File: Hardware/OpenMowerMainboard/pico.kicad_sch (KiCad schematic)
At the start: 3 parts, among them U10 74HC4051, U11 Pico, U9 74HC4051

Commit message: wip schematic
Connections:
- net USS_ADDRESS_0 renamed MUX_ADDRESS_0
- net USS_ADDRESS_1 renamed MUX_ADDRESS_1
- net USS_ADDRESS_2 renamed MUX_ADDRESS_2
- net USS_ECHO renamed MUX_INPUT
- net USS_TRIGGER renamed MUX_OUTPUT
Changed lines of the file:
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@@
     (stroke (width 0) (type default) (color 0 0 0 0))
   )
-  (label "USS_ADDRESS_0" (at 173.99 88.9 0)
+  (label "MUX_ADDRESS_0" (at 173.99 88.9 0)
     (effects (font (size 1.27 1.27)) (justify left bottom))
   )
-  (label "USS_TRIGGER" (at 69.85 86.36 0)
+  (label "MUX_OUTPUT" (at 69.85 86.36 0)
     (effects (font (size 1.27 1.27)) (justify left bottom))
   )
-  (label "USS_ADDRESS_2" (at 131.445 96.52 0)
+  (label "MUX_ADDRESS_2" (at 131.445 96.52 0)
     (effects (font (size 1.27 1.27)) (justify left bottom))
   )
-  (label "USS_ADDRESS_0" (at 131.445 91.44 0)
+  (label "MUX_ADDRESS_0" (at 131.445 91.44 0)
     (effects (font (size 1.27 1.27)) (justify left bottom))
   )
-  (label "USS_ADDRESS_0" (at 69.85 91.44 0)
+  (label "MUX_ADDRESS_0" (at 69.85 91.44 0)
     (effects (font (size 1.27 1.27)) (justify left bottom))
   )
-  (label "USS_ADDRESS_2" (at 69.85 96.52 0)
+  (label "MUX_ADDRESS_2" (at 69.85 96.52 0)
     (effects (font (size 1.27 1.27)) (justify left bottom))
   )
-  (label "USS_ECHO" (at 131.445 86.36 0)
+  (label "MUX_INPUT" (at 131.445 86.36 0)
     (effects (font (size 1.27 1.27)) (justify left bottom))
   )
-  (label "USS_TRIGGER" (at 173.99 76.2 0)
+  (label "MUX_OUTPUT" (at 173.99 76.2 0)
     (effects (font (size 1.27 1.27)) (justify left bottom))
   )
-  (label "USS_ADDRESS_2" (at 173.99 93.98 0)
+  (label "MUX_ADDRESS_2" (at 173.99 93.98 0)
     (effects (font (size 1.27 1.27)) (justify left bottom))
   )
-  (label "USS_ECHO" (at 173.99 78.74 0)
+  (label "MUX_INPUT" (at 173.99 78.74 0)
     (effects (font (size 1.27 1.27)) (justify left bottom))
   )
-  (label "USS_ADDRESS_1" (at 173.99 91.44 0)
+  (label "MUX_ADDRESS_1" (at 173.99 91.44 0)
     (effects (font (size 1.27 1.27)) (justify left bottom))
   )
-  (label "USS_ADDRESS_1" (at 69.85 93.98 0)
+  (label "MUX_ADDRESS_1" (at 69.85 93.98 0)
     (effects (font (size 1.27 1.27)) (justify left bottom))
   )
-  (label "USS_ADDRESS_1" (at 131.445 93.98 0)
+  (label "MUX_ADDRESS_1" (at 131.445 93.98 0)
     (effects (font (size 1.27 1.27)) (justify left bottom))
   )

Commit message: added footprints to schematic
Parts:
- U10, U9: footprint (none) -> Package_SO:SSOP-16_4.4x5.2mm_P0.65mm
- U11: footprint RPi_Pico:RPi_Pico_SMD_TH -> MCU_RaspberryPi_and_Boards:RPi_Pico_SMD_TH
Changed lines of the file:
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@@
       (effects (font (size 1.27 1.27)) (justify right))
     )
-    (property "Footprint" "" (id 2) (at 52.07 104.14 0)
+    (property "Footprint" "Package_SO:SSOP-16_4.4x5.2mm_P0.65mm" (id 2) (at 52.07 104.14 0)
       (effects (font (size 1.27 1.27)) hide)
     )
@@
       (effects (font (size 1.27 1.27)) (justify left))
     )
-    (property "Footprint" "" (id 2) (at 113.665 104.14 0)
+    (property "Footprint" "Package_SO:SSOP-16_4.4x5.2mm_P0.65mm" (id 2) (at 113.665 104.14 0)
       (effects (font (size 1.27 1.27)) hide)
     )
@@
     (property "Reference" "U11" (id 0) (at 215.9 60.96 0))
     (property "Value" "Pico" (id 1) (at 215.9 63.5 0))
-    (property "Footprint" "RPi_Pico:RPi_Pico_SMD_TH" (id 2) (at 215.9 92.71 90)
+    (property "Footprint" "MCU_RaspberryPi_and_Boards:RPi_Pico_SMD_TH" (id 2) (at 215.9 92.71 90)
       (effects (font (size 1.27 1.27)) hide)
     )

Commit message: wip
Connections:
- net MUX_INPUT: now also U11.4 (GPIO2); no longer U11.5 (GPIO3)
- net MUX_OUTPUT: now also U11.5 (GPIO3); no longer U11.4 (GPIO2)
- net USS_1_ECHO: now also U10.15 (A2); no longer U10.13 (A0)
- net USS_1_TRIGGER: now also U9.15 (A2); no longer U9.13 (A0)
- net USS_3_ECHO: now also U10.13 (A0); no longer U10.15 (A2)
- net USS_3_TRIGGER: now also U9.13 (A0); no longer U9.15 (A2)

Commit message: wip pcb layout
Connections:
- net GPS_POWER: now also U11.29 (GPIO22); no longer U11.12 (GPIO9)
- net HALL_SWITCH_1: now also U11.10 (GPIO7); no longer U11.19 (GPIO14)
- net HALL_SWITCH_2: now also U11.9 (GPIO6); no longer U11.20 (GPIO15)
- net HALL_SWITCH_3: now also U11.5 (GPIO3); no longer U11.27 (GPIO21)
- net HALL_SWITCH_4: now also U11.4 (GPIO2); no longer U11.29 (GPIO22)
- net MUX_ADDRESS_0: now also U11.17 (GPIO13); no longer U11.9 (GPIO6)
- net MUX_ADDRESS_1: now also U11.19 (GPIO14); no longer U11.10 (GPIO7)
- net MUX_ADDRESS_2: now also U11.20 (GPIO15); no longer U11.11 (GPIO8)
- net MUX_INPUT: now also U11.15 (GPIO11); no longer U11.4 (GPIO2)
- net MUX_OUTPUT: now also U11.16 (GPIO12); no longer U11.5 (GPIO3)
- net RASPI_POWER: now also U11.27 (GPIO21); no longer U11.14 (GPIO10)
- net SOUND_CLK: now also U11.11 (GPIO8); no longer U11.15 (GPIO11)
- net SOUND_DATA: now also U11.12 (GPIO9); no longer U11.16 (GPIO12)
- net SOUND_RESET: now also U11.14 (GPIO10); no longer U11.17 (GPIO13)

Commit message: WIP hardware revision
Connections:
- net ESC_POWER: no longer names the net of U11.26 (GPIO20)
- net GPS_POWER renamed ENABLE_CHARGE
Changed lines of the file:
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@@
     (stroke (width 0) (type default) (color 0 0 0 0))
   )
-  (wire (pts (xy 257.81 96.52) (xy 233.68 96.52))
+  (wire (pts (xy 254 96.52) (xy 233.68 96.52))
     (stroke (width 0) (type default) (color 0 0 0 0))
   )
@@
     (effects (font (size 1.27 1.27)) (justify right))
   )
-  (hierarchical_label "RASPI_POWER" (shape output) (at 254 101.6 0)
-    (effects (font (size 1.27 1.27)) (justify left))
-  )
   (hierarchical_label "IMU_MISO" (shape input) (at 254 116.84 0)
     (effects (font (size 1.27 1.27)) (justify left))
@@
     (effects (font (size 1.27 1.27)) (justify left))
   )
+  (hierarchical_label "RASPI_POWER" (shape output) (at 254 101.6 0)
+    (effects (font (size 1.27 1.27)) (justify left))
+  )
   (hierarchical_label "SWDIO" (shape bidirectional) (at 218.44 132.08 270)
     (effects (font (size 1.27 1.27)) (justify right))
@@
     (effects (font (size 1.27 1.27)) (justify left))
   )
-  (hierarchical_label "ESC_POWER" (shape output) (at 254 104.14 0)
-    (effects (font (size 1.27 1.27)) (justify left))
-  )
   (hierarchical_label "HALL_SWITCH_1" (shape input) (at 173.99 91.44 180)
     (effects (font (size 1.27 1.27)) (justify right))
@@
   (hierarchical_label "USS_4_ECHO" (shape input) (at 100.33 93.98 180)
     (effects (font (size 1.27 1.27)) (justify right))
-  )
-  (hierarchical_label "GPS_POWER" (shape output) (at 257.81 96.52 0)
-    (effects (font (size 1.27 1.27)) (justify left))
   )
   (hierarchical_label "SOUND_DATA" (shape output) (at 173.99 96.52 180)
@@
     (effects (font (size 1.27 1.27)) (justify right))
   )
+  (hierarchical_label "ENABLE_CHARGE" (shape output) (at 254 96.52 0)
+    (effects (font (size 1.27 1.27)) (justify left))
+  )
   (hierarchical_label "USS_5_TRIGGER" (shape output) (at 27.305 96.52 180)

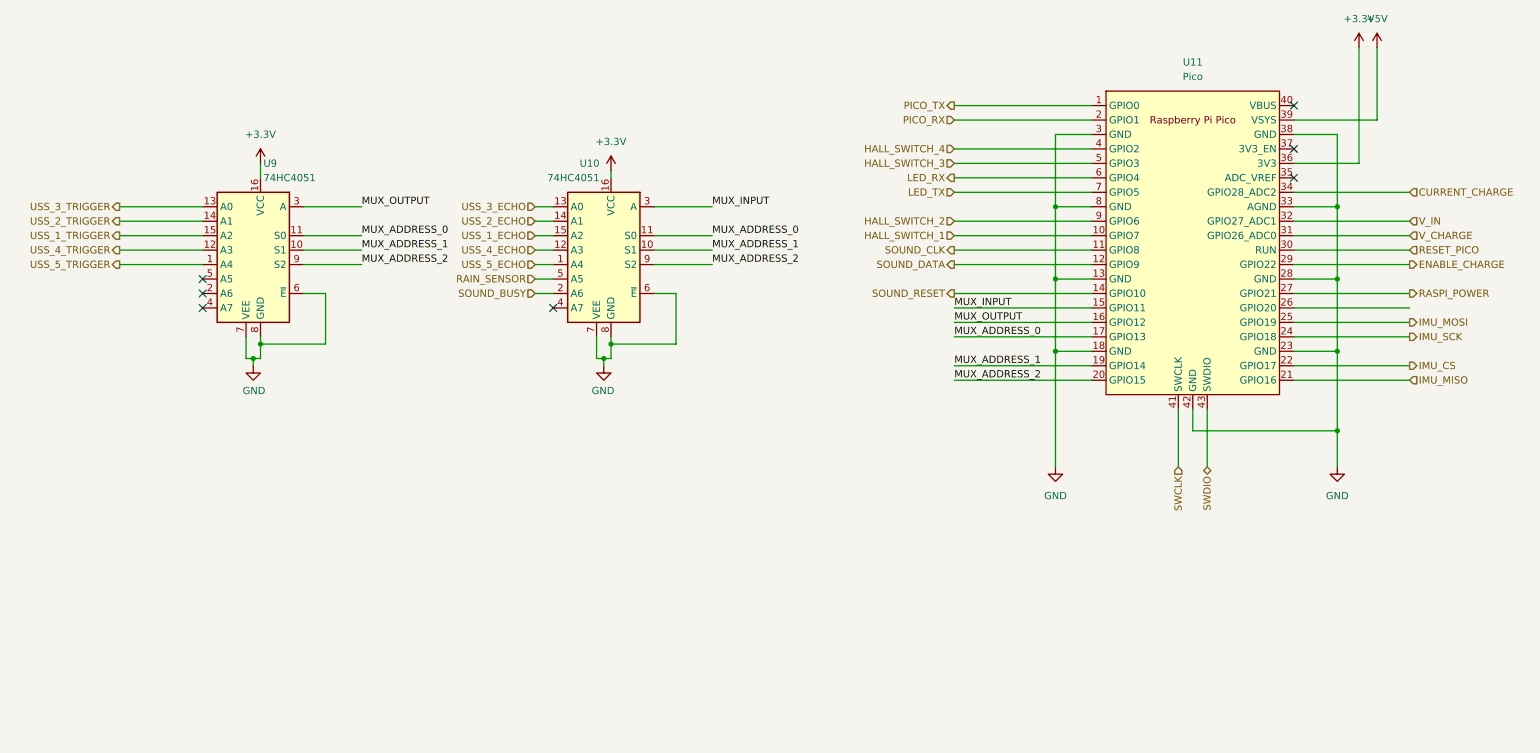
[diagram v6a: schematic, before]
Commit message: v0_9_1 mainboard rework
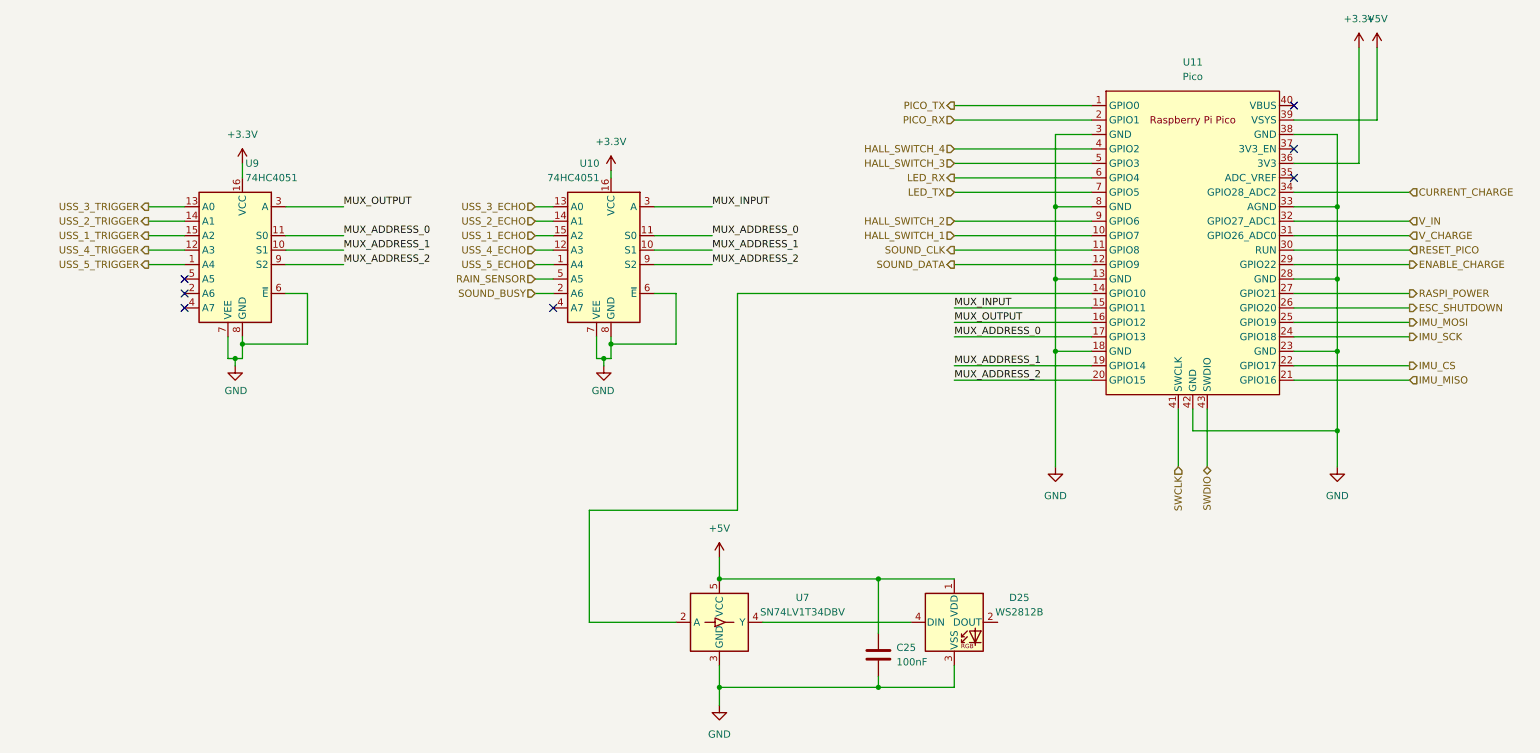
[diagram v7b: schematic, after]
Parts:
- added C25: 100nF, Capacitor_SMD:C_0805_2012Metric_Pad1.18x1.45mm_HandSolder, symbol Device:C
- added D25: WS2812B, LED_SMD:LED_WS2812B_PLCC4_5.0x5.0mm_P3.2mm, symbol LED:WS2812B
- added U7: SN74LV1T34DBV, Package_TO_SOT_SMD:SOT-23-5, symbol Logic_LevelTranslator:SN74LV1T34DBV
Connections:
- net +5V: now also C25.1, D25.1 (VDD), U7.5 (VCC)
- net GND: now also C25.2, D25.3 (VSS), U7.3 (GND)
- net ESC_SHUTDOWN: now reaches U11.26 (GPIO20)
- net SOUND_RESET: no longer names the net of U11.14 (GPIO10)
- net SOUND_RESET: now also U7.2 (A)
- new net: D25.4 (DIN), U7.4 (Y)
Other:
- moved on the sheet: U9
